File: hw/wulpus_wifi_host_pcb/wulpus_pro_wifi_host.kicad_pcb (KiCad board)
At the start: 2 copper layers, 39 x 20.9 mm, 2 parts, among them J1 DF40C-50DP-0.4V_51_, U1 XIAO-ESP32-C6-SMD

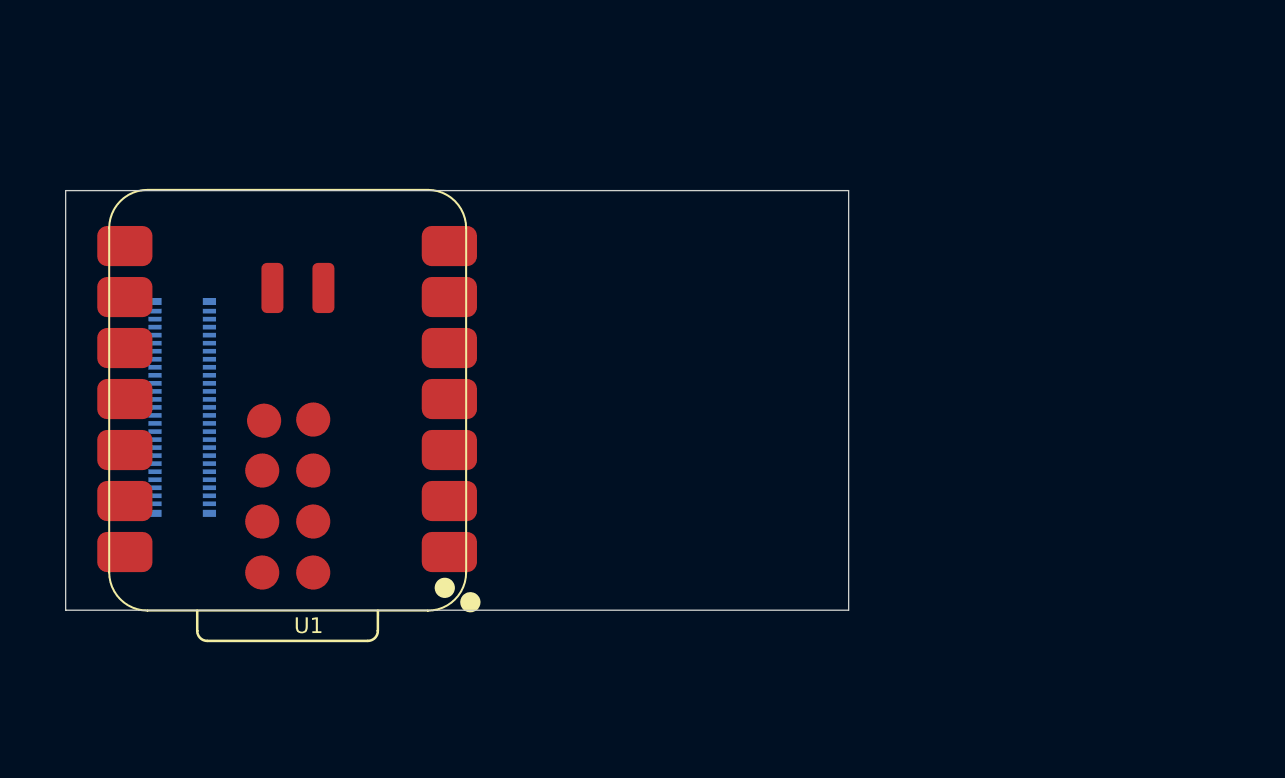
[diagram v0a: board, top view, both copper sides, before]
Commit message: Added main ICs to the schematics and layout template
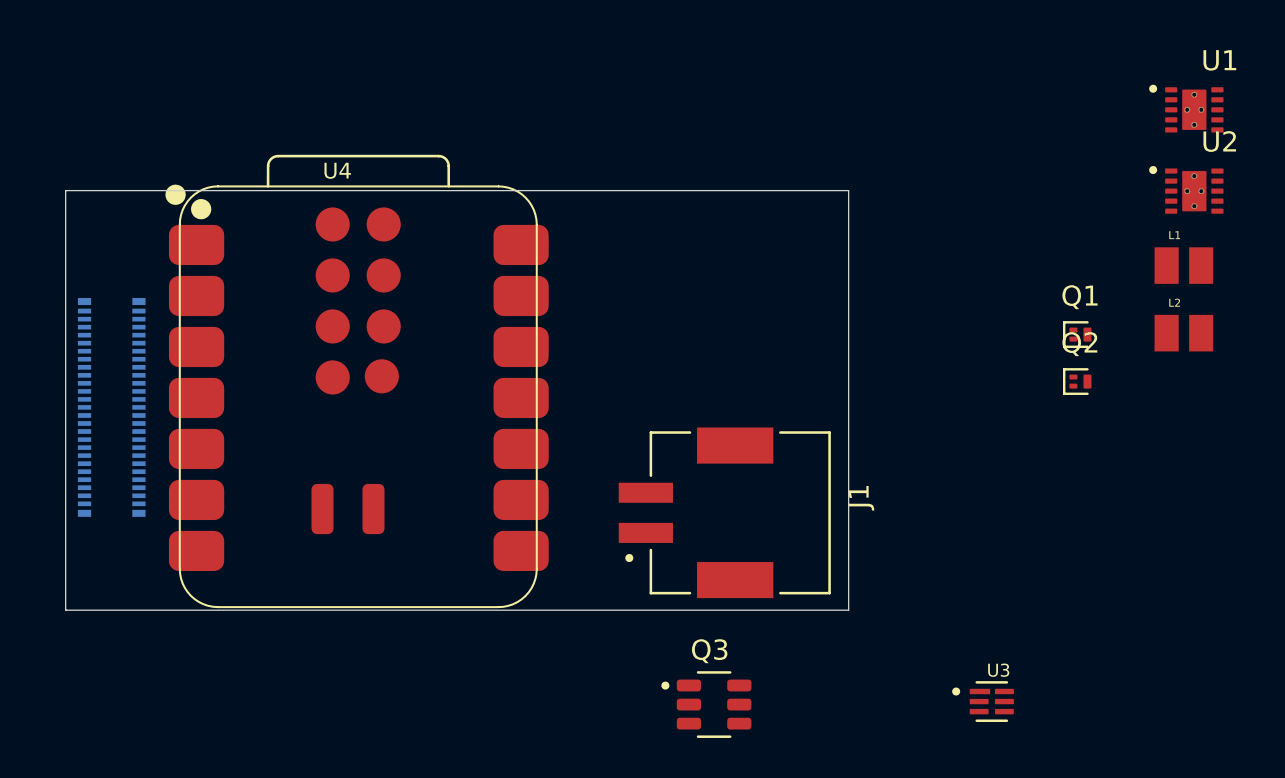
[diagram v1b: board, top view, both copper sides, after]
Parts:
- added J2: DF40C-50DP-0.4V_51_, Ultrasound:HIROSE_DF40C-50DP-0.4V_51_, B.Cu at (67.3, 90.9)
- added L1: DFE201612E-2R2M=P2, Ultrasound:INDC2016X120N, F.Cu at (120.7, 83.8)
- added L2: DFE201612E-2R2M=P2, Ultrasound:INDC2016X120N, F.Cu at (120.7, 87.2)
- added Q1: LP0404N3T5G, Package_TO_SOT_SMD:SOT-883, F.Cu at (115.5, 87.3)
- added Q2: LP0404N3T5G, Package_TO_SOT_SMD:SOT-883, F.Cu at (115.5, 89.6)
- added Q3: FS8205A, Ultrasound:SOT95P280X145-6N, F.Cu at (97.3, 105.7)
- added U2: TPS63900DSKR, Ultrasound:IC_TPS63900DSKR, F.Cu at (121.2, 80.1)
- added U3: BQ29700DSER, Ultrasound:SON50P150X150X80-6N, F.Cu at (111.1, 105.5)
- added U4: XIAO-ESP32-C6-SMD, Ultrasound:XIAO-ESP32-C6-SMD, F.Cu at (70.7, 100.9)
- J1: value DF40C-50DP-0.4V_51_ -> SM02B-PASS-TBT_LF__SN_; footprint Ultrasound:HIROSE_DF40C-50DP-0.4V_51_ -> Ultrasound:JST_SM02B-PASS-TBT_LF__SN_; moved to F.Cu
- U1: value XIAO-ESP32-C6-SMD -> TPS63900DSKR; footprint Ultrasound:XIAO-ESP32-C6-SMD -> Ultrasound:IC_TPS63900DSKR
- moved U1 36.5 mm to (121.2, 76.1), turned to 0 degrees
- moved J1 27.5 mm to (97.8, 96.2)
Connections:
- U1 pad 12: unconnected-(U1-3V3_OUT-Pad12) -> (no net)
- U1 pad 13: unconnected-(U1-GND-Pad13) -> (no net)
- U1 pad 14: unconnected-(U1-VBUS-Pad14) -> (no net)
- U1 pad 15: unconnected-(U1-MTDI-Pad15) -> (no net)

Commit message: Updated footprints, mapped 3D models, added layerstack, partial placement and layout
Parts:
- removed the Q2 at (115.5, 89.6)
- added C1: 22 uF, Capacitor_SMD:C_0402_1005Metric, F.Cu at (99.0, 96.3)
- added C2: 10 uF, Capacitor_SMD:C_0402_1005Metric, F.Cu at (103.0, 95.2)
- added C3: 0.1uF, Capacitor_SMD:C_0402_1005Metric, B.Cu at (94.5, 84.8)
- added C4: 22 uF, Capacitor_SMD:C_0402_1005Metric, F.Cu at (92.8, 96.3)
- added C5: 10 uF, Capacitor_SMD:C_0402_1005Metric, F.Cu at (96.8, 95.2)
- added C6: 100 nF, Capacitor_SMD:C_0402_1005Metric, F.Cu at (90.5, 81.7)
- added C7: 10 uF, Capacitor_SMD:C_0402_1005Metric, B.Cu at (71.5, 94.6)
- added C8: 10 uF, Capacitor_SMD:C_0402_1005Metric, B.Cu at (71.7, 91.5)
- added D1: LMBR4010BST5G, Diode_SMD:D_SOD-882, F.Cu at (90.5, 83.5)
- added R1: 47, Resistor_SMD:R_0402_1005Metric, F.Cu at (68.7, 81.8)
- added R10: 47, Resistor_SMD:R_0402_1005Metric, B.Cu at (72.1, 84.1)
- added R11: 47, Resistor_SMD:R_0402_1005Metric, B.Cu at (72.1, 85.4)
- added R12: 0, Resistor_SMD:R_0402_1005Metric, F.Cu at (101.0, 92.8)
- added R13: o, Resistor_SMD:R_0402_1005Metric, F.Cu at (100.0, 92.8)
- added R14: 2.2k, Resistor_SMD:R_0402_1005Metric, B.Cu at (91.9, 82.1)
- added R15: 16.2k, Resistor_SMD:R_0402_1005Metric, F.Cu at (99.0, 93.8)
- added R16: 5.1M, Resistor_SMD:R_0402_1005Metric, B.Cu at (100.7, 81.5)
- added R17: 5.1M, Resistor_SMD:R_0402_1005Metric, B.Cu at (100.8, 84.1)
- added R18: 0, Resistor_SMD:R_0402_1005Metric, F.Cu at (94.7, 92.8)
- added R19: 330, Resistor_SMD:R_0402_1005Metric, B.Cu at (94.3, 85.8)
- added R2: 47, Resistor_SMD:R_0402_1005Metric, B.Cu at (71.9, 90.0)
- added R20: o, Resistor_SMD:R_0402_1005Metric, F.Cu at (93.8, 92.8)
- added R21: 36.5k, Resistor_SMD:R_0402_1005Metric, F.Cu at (92.8, 93.8)
- added R22: 100k, Resistor_SMD:R_0402_1005Metric, F.Cu at (91.8, 82.5)
- added R23: 100, Resistor_SMD:R_0402_1005Metric, F.Cu at (92.8, 83.3)
- added R3: 47, Resistor_SMD:R_0402_1005Metric, F.Cu at (69.2, 87.5)
- added R4: 47, Resistor_SMD:R_0402_1005Metric, F.Cu at (69.2, 90.0)
- added R5: 47, Resistor_SMD:R_0402_1005Metric, F.Cu at (69.1, 92.6)
- added R6: 47, Resistor_SMD:R_0402_1005Metric, F.Cu at (69.1, 95.1)
- added R7: 47, Resistor_SMD:R_0402_1005Metric, F.Cu at (68.6, 98.2)
- added R8: 47, Resistor_SMD:R_0402_1005Metric, B.Cu at (72.1, 82.8)
- added R9: 47, Resistor_SMD:R_0402_1005Metric, B.Cu at (72.1, 81.4)
- added TP1: TestPoint, TestPoint:TestPoint_Pad_1.0x1.0mm, F.Cu at (98.4, 98.9)
- added TP2: TestPoint, TestPoint:TestPoint_Pad_1.0x1.0mm, F.Cu at (92.2, 98.8)
- added TP3: TestPoint, TestPoint:TestPoint_Pad_1.0x1.0mm, F.Cu at (110.7, 89.0)
- added TP4: TestPoint, TestPoint:TestPoint_Pad_1.0x1.0mm, F.Cu at (67.8, 84.7)
- added TP5: TestPoint, TestPoint:TestPoint_Pad_1.0x1.0mm, F.Cu at (107.0, 89.3)
- J1: value SM02B-PASS-TBT_LF__SN_ -> S2B-PH-SM4-TB_LF__SN_; footprint Ultrasound:JST_SM02B-PASS-TBT_LF__SN_ -> Ultrasound:JST_S2B-PH-SM4-TB_LF__SN_
- Q1: renamed from Q3; moved to B.Cu
- U3: moved to B.Cu
- moved U4 32.8 mm to (94.8, 95.5), turned to -90 degrees
- moved U3 29.3 mm to (93.9, 81.8), turned to -90 degrees
- moved L2 28.2 mm to (95.0, 98.8)
- moved U2 25.4 mm to (101.0, 95.5), turned to -90 degrees
- moved L1 24.7 mm to (101.1, 98.8)
- moved Q2 24.0 mm to (91.8, 84.3), turned to -90 degrees
- moved Q1 23.7 mm to (97.3, 82.0)
- moved J1 8.38 mm to (98.5, 87.8), turned to 180 degrees
- moved J2 0.97 mm to (67.7, 90.0)
- moved U1 0.32 mm to (71.0, 101.1)
- renumbered Q1 to Q2, U4 to U1, U1 to U4
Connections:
- J1 pad 1: unconnected-(J1-Pad1) -> /Power/VBAT
- J1 pad 2: unconnected-(J1-Pad2) -> Net-(U3-VSS)
- J1 pad S1: Net-(J1-SHIELD-PadS1) -> GND
- J1 pad S2: Net-(J1-SHIELD-PadS1) -> GND
- J2 pad 1: unconnected-(J2-Pad1) -> /b2b_connector Sheet/SPI.MOSI
- J2 pad 15: unconnected-(J2-Pad15) -> GND
- J2 pad 16: unconnected-(J2-Pad16) -> GND
- J2 pad 2: unconnected-(J2-Pad2) -> /b2b_connector Sheet/SPI.MISO
- J2 pad 22: unconnected-(J2-Pad22) -> /b2b_connector Sheet/MSP_JTAG.TEST
- J2 pad 24: unconnected-(J2-Pad24) -> Net-(J2-Pad24)
- J2 pad 25: unconnected-(J2-Pad25) -> /b2b_connector Sheet/data_rdy
- J2 pad 26: unconnected-(J2-Pad26) -> /b2b_connector Sheet/MSP_JTAG.TDO
- J2 pad 28: unconnected-(J2-Pad28) -> /b2b_connector Sheet/MSP_JTAG.TDI
- J2 pad 29: unconnected-(J2-Pad29) -> +3V3
- J2 pad 3: unconnected-(J2-Pad3) -> /b2b_connector Sheet/SPI.SS
- J2 pad 30: unconnected-(J2-Pad30) -> /b2b_connector Sheet/MSP_JTAG.TMS
- J2 pad 31: unconnected-(J2-Pad31) -> +3V3
- J2 pad 33: unconnected-(J2-Pad33) -> +5V
- J2 pad 36: unconnected-(J2-Pad36) -> GND
- J2 pad 37: unconnected-(J2-Pad37) -> +3V3 ESP
- J2 pad 39: unconnected-(J2-Pad39) -> +3V3 ESP
- J2 pad 4: unconnected-(J2-Pad4) -> /b2b_connector Sheet/SPI.CLK
- J2 pad 47: unconnected-(J2-Pad47) -> +V_board
- J2 pad 48: unconnected-(J2-Pad48) -> /b2b_connector Sheet/MSP_JTAG.TCK
- J2 pad 49: unconnected-(J2-Pad49) -> +V_board
- J2 pad 50: unconnected-(J2-Pad50) -> /b2b_connector Sheet/MSP_JTAG.RST_n
- L1 pad 1: unconnected-(L1-Pad1) -> Net-(U2-LX2)
- L1 pad 2: unconnected-(L1-Pad2) -> Net-(U2-LX1)
- L2 pad 1: unconnected-(L2-Pad1) -> Net-(U4-LX2)
- L2 pad 2: unconnected-(L2-Pad2) -> Net-(U4-LX1)
- Q1 pad 1: unconnected-(Q3-Pad1) -> Net-(U3-VSS)
- Q1 pad 3: unconnected-(Q3-Pad3) -> GND
- Q1 pad 4: unconnected-(Q3-Pad4) -> Net-(U3-COUT)
- Q1 pad 6: unconnected-(Q3-Pad6) -> Net-(U3-DOUT)
- Q2 pad 1: unconnected-(Q1-G-Pad1) -> Net-(Q2-G)
- Q2 pad 2: unconnected-(Q1-S-Pad2) -> +V_board
- Q2 pad 3: unconnected-(Q1-D-Pad3) -> /Power/VBAT
- U1 pad 1: unconnected-(U4-D0-Pad1) -> Net-(U1-D0)
- U1 pad 10: unconnected-(U4-D9-Pad10) -> Net-(U1-D9)
- U1 pad 11: unconnected-(U4-D10-Pad11) -> Net-(U1-D10)
- U1 pad 12: unconnected-(U4-3V3_OUT-Pad12) -> +3V3 ESP
- U1 pad 13: unconnected-(U4-GND-Pad13) -> GND
- U1 pad 14: unconnected-(U4-VBUS-Pad14) -> /Power/VBUS
- U1 pad 2: unconnected-(U4-D1-Pad2) -> Net-(U1-D1)
- U1 pad 23: unconnected-(U4-VBAT-Pad23) -> /Power/VBAT
- U1 pad 24: unconnected-(U4-GND-Pad24) -> GND
- U1 pad 3: unconnected-(U4-D2-Pad3) -> Net-(U1-D2)
- U1 pad 4: unconnected-(U4-D3-Pad4) -> Net-(U1-D3)
- U1 pad 5: unconnected-(U4-D4-Pad5) -> Net-(U1-D4)
- U1 pad 6: unconnected-(U4-D5-Pad6) -> Net-(U1-D5)
- U1 pad 7: unconnected-(U4-D6-Pad7) -> Net-(U1-D6)
- U1 pad 8: unconnected-(U4-D7-Pad8) -> Net-(U1-D7)
- U1 pad 9: unconnected-(U4-D8-Pad9) -> Net-(U1-D8)
- U2 pad 1: unconnected-(U2-EN-Pad1) -> +V_board
- U2 pad 10: unconnected-(U2-VIN-Pad10) -> +V_board
- U2 pad 11: unconnected-(U2-EXP-Pad11) -> GND
- U2 pad 2: unconnected-(U2-SEL-Pad2) -> GND
- U2 pad 3: unconnected-(U2-CFG1-Pad3) -> Net-(U2-CFG1)
- U2 pad 4: unconnected-(U2-CFG2-Pad4) -> Net-(U2-CFG2)
- U2 pad 5: unconnected-(U2-CFG3-Pad5) -> Net-(U2-CFG3)
- U2 pad 6: unconnected-(U2-VOUT-Pad6) -> +3V3
- U2 pad 7: unconnected-(U2-LX2-Pad7) -> Net-(U2-LX2)
- U2 pad 8: unconnected-(U2-GND-Pad8) -> GND
- U2 pad 9: unconnected-(U2-LX1-Pad9) -> Net-(U2-LX1)
- U3 pad 2: unconnected-(U3-COUT-Pad2) -> Net-(U3-COUT)
- U3 pad 3: unconnected-(U3-DOUT-Pad3) -> Net-(U3-DOUT)
- U3 pad 4: unconnected-(U3-VSS-Pad4) -> Net-(U3-VSS)
- U3 pad 5: unconnected-(U3-BAT-Pad5) -> Net-(U3-BAT)
- U3 pad 6: unconnected-(U3-V--Pad6) -> Net-(U3-V-)
- U4 pad 1: unconnected-(U1-EN-Pad1) -> +V_board
- U4 pad 10: unconnected-(U1-VIN-Pad10) -> +V_board
- U4 pad 11: unconnected-(U1-EXP-Pad11) -> GND
- U4 pad 2: unconnected-(U1-SEL-Pad2) -> GND
- U4 pad 3: unconnected-(U1-CFG1-Pad3) -> Net-(U4-CFG1)
- U4 pad 4: unconnected-(U1-CFG2-Pad4) -> Net-(U4-CFG2)
- U4 pad 5: unconnected-(U1-CFG3-Pad5) -> Net-(U4-CFG3)
- U4 pad 6: unconnected-(U1-VOUT-Pad6) -> +5V
- U4 pad 7: unconnected-(U1-LX2-Pad7) -> Net-(U4-LX2)
- U4 pad 8: unconnected-(U1-GND-Pad8) -> GND
- U4 pad 9: unconnected-(U1-LX1-Pad9) -> Net-(U4-LX1)
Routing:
- net /Power/VBAT: track 0.00 -> 39.5 mm
- net Net-(U1-D9): track 0.00 -> 25.1 mm, vias 0 -> 1
- net Net-(U1-D7): track 0.00 -> 24.0 mm, vias 0 -> 1
- net Net-(U1-D8): track 0.00 -> 23.6 mm, vias 0 -> 1
- net Net-(U1-D10): track 0.00 -> 23.4 mm, vias 0 -> 1
- net /b2b_connector Sheet/MSP_JTAG.RST_n: track 0.00 -> 16.5 mm, vias 0 -> 1
- net /b2b_connector Sheet/SPI.MISO: track 0.00 -> 7.65 mm
- net /b2b_connector Sheet/SPI.CLK: track 0.00 -> 6.92 mm
- net Net-(J2-Pad24): track 0.00 -> 6.87 mm, vias 0 -> 1
- net Net-(U1-D1): track 0.00 -> 5.99 mm, vias 0 -> 1
- net /b2b_connector Sheet/MSP_JTAG.TMS: track 0.00 -> 5.22 mm, vias 0 -> 1
- net /b2b_connector Sheet/MSP_JTAG.TCK: track 0.00 -> 5.04 mm, vias 0 -> 1
- net /b2b_connector Sheet/MSP_JTAG.TEST: track 0.00 -> 3.85 mm, vias 0 -> 1
- net /b2b_connector Sheet/MSP_JTAG.TDI: track 0.00 -> 3.45 mm, vias 0 -> 1
- net Net-(U1-D0): track 0.00 -> 3.15 mm
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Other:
- board size 39 x 20.9 mm -> 39 x 21 mm
- copper layers 2 -> 4

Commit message: Added preliminary layout
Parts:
- moved TP3 14.0 mm to (97.0, 92.2)
- moved TP5 4.89 mm to (102.2, 90.0)
- moved R14 3.22 mm to (93.7, 84.8)
- moved U3 3.21 mm to (95.5, 84.7)
- moved Q1 3.18 mm to (99.3, 84.5)
- moved R17 3.06 mm to (99.3, 86.8)
- moved C3 3.01 mm to (95.3, 87.7)
- moved R16 1.52 mm to (99.4, 82.3), turned to 180 degrees
- moved C6 1.45 mm to (90.5, 83.2)
- moved D1 1.45 mm to (90.5, 84.9)
- moved Q2 1.45 mm to (91.8, 85.8)
- moved R23 1.45 mm to (92.8, 84.8)
- moved R22 1.45 mm to (91.8, 84.0)
- moved R15 1.00 mm to (99.0, 92.8)
- moved C1 0.82 mm to (98.9, 95.5)
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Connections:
- U2 pad 12: (no net) -> GND
- U2 pad 13: (no net) -> GND
- U4 pad 12: (no net) -> GND
- U4 pad 13: (no net) -> GND
- U4 pad 14: (no net) -> GND
- U4 pad 15: (no net) -> GND
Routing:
- net Net-(U3-DOUT): track 0.00 -> 11.5 mm, vias 0 -> 2
- net Net-(Q1-Pad2): track 0.00 -> 10.3 mm, vias 0 -> 1
- net Net-(U3-COUT): track 0.00 -> 9.61 mm
- net GND: track 0.00 -> 6.19 mm, vias 0 -> 43
- net +5V: track 0.00 -> 6.02 mm, vias 0 -> 2
- net +V_board: track 0.00 -> 5.28 mm, vias 0 -> 12
- net +3V3 ESP: track 0.00 -> 5.26 mm, vias 0 -> 4
- net Net-(U3-VSS): track 0.00 -> 3.71 mm, vias 0 -> 7
- net +3V3: track 0.00 -> 3.22 mm, vias 0 -> 4
- net Net-(U3-BAT): track 0.00 -> 2.64 mm
- net Net-(U2-CFG3): track 0.00 -> 1.44 mm
- net Net-(U4-CFG2): track 0.00 -> 1.32 mm
- net Net-(U3-V-): track 0.00 -> 1.26 mm
- net Net-(U2-CFG2): track 0.00 -> 1.22 mm
- net Net-(U4-CFG1): track 0.00 -> 1.13 mm
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- added copper zone on B.Cu, net +3V3
- added copper zone on F.Cu, net +3V3
- added copper zone on In2.Cu, net +3V3
- added copper zone on B.Cu, net +3V3 ESP
- added copper zone on In2.Cu, net +3V3 ESP
- added copper zone on In2.Cu, net +5V
- added copper zone on B.Cu, net +V_board
- added copper zone on F.Cu, net +V_board
- added copper zone on In2.Cu, net +V_board
- added copper zone on F.Cu, net /Power/VBUS
- added copper zone on B.Cu, net GND
- added copper zone on F.Cu, net GND
- added copper zone on In1.Cu, net GND
- added copper zone on In2.Cu, net GND
- added copper zone on F.Cu, net Net-(U2-LX1)
- added copper zone on F.Cu, net Net-(U2-LX2)
- added copper zone on B.Cu, net Net-(U3-VSS)
- added copper zone on F.Cu, net Net-(U3-VSS)
- added copper zone on F.Cu, net Net-(U4-LX1)
- added copper zone on F.Cu, net Net-(U4-LX2)
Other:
- rule pad_to_mask_clearance: 0 -> 0.1

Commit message: Finished layout, fixed DRCs
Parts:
- added QR*****: https://github.com/Sergio5714/wulpus-pro, Ultrasound:wulpus_pro_qr, B.Cu at (83.0, 86.9)
- added TP6: TestPoint, TestPoint:TestPoint_Pad_1.0x1.0mm, F.Cu at (91.5, 90.7)
- added TP7: TestPoint, TestPoint:TestPoint_Pad_1.0x1.0mm, F.Cu at (66.6, 97.1)
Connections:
- U2 pad 14: (no net) -> GND
- U2 pad 15: (no net) -> GND
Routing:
- net GND: track 6.19 -> 4.77 mm
- net +3V3 ESP: track 5.26 -> 4.21 mm
- net /Power/VBAT: track 40.3 -> 39.3 mm
- net Net-(U1-D3): track 3.14 -> 2.28 mm
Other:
- board text added: "WiFi Host Board v1.0 Sergei Vostrikov 29.07.26"

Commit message: Changed cap footprints to 0603
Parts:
- C1, C2, C4, C5, C7, C8: footprint Capacitor_SMD:C_0402_1005Metric -> Capacitor_SMD:C_0603_1608Metric
- R13, R20: value o -> 0
- moved C4 1.32 mm to (91.8, 95.4)
- moved R21 1.17 mm to (92.1, 92.8)
- moved TP2 0.78 mm to (91.4, 98.9)
- moved L2 0.72 mm to (94.2, 98.9)
- moved R18 0.72 mm to (94.0, 92.8)
- moved R20 0.72 mm to (93.0, 92.8)
- moved U4 0.72 mm to (94.1, 95.6)
- moved C1 0.62 mm to (98.4, 95.3)
- moved TP3 0.59 mm to (96.5, 92.2)
- moved C5 0.51 mm to (96.3, 95.3)
- moved TP1 0.44 mm to (98.0, 98.9)
- moved L1 0.44 mm to (100.7, 98.9)
- moved R12 0.44 mm to (100.6, 92.9)
- moved R13 0.44 mm to (99.6, 92.9)
- moved R15 0.44 mm to (98.6, 92.9)
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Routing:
- net +V_board: track 5.22 -> 7.71 mm, vias 12 -> 11
- net +5V: track 6.02 -> 4.70 mm
- net Net-(U4-CFG3): track 0.96 -> 1.52 mm
- net GND: vias 43 -> 47
- added copper zone on F.Cu, net +5V
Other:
- board text added: "WiFi Host Board v1.0 Sergei Vostrikov 30.07.26"
- board text removed: "WiFi Host Board v1.0 Sergei Vostrikov 29.07.26"

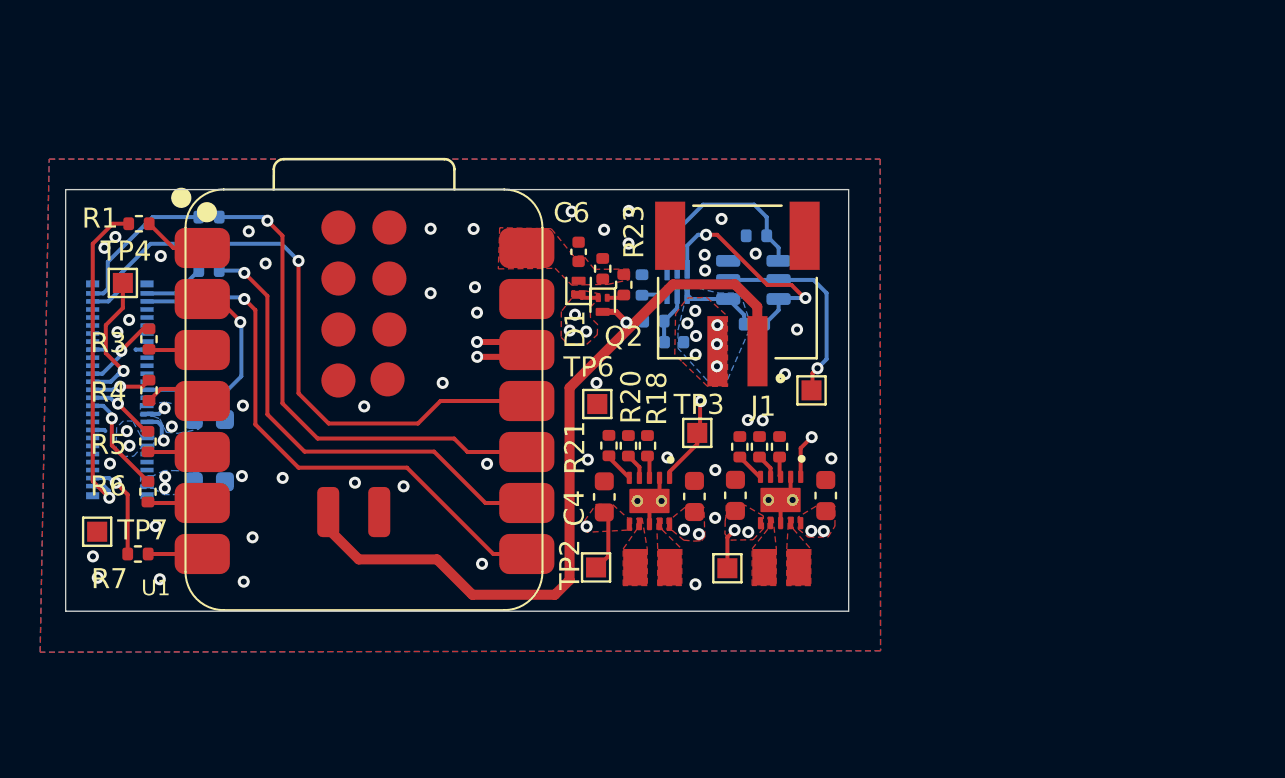
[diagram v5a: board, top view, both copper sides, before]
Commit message: Added out capacitors for DC-DCs, regenerated fabrication files
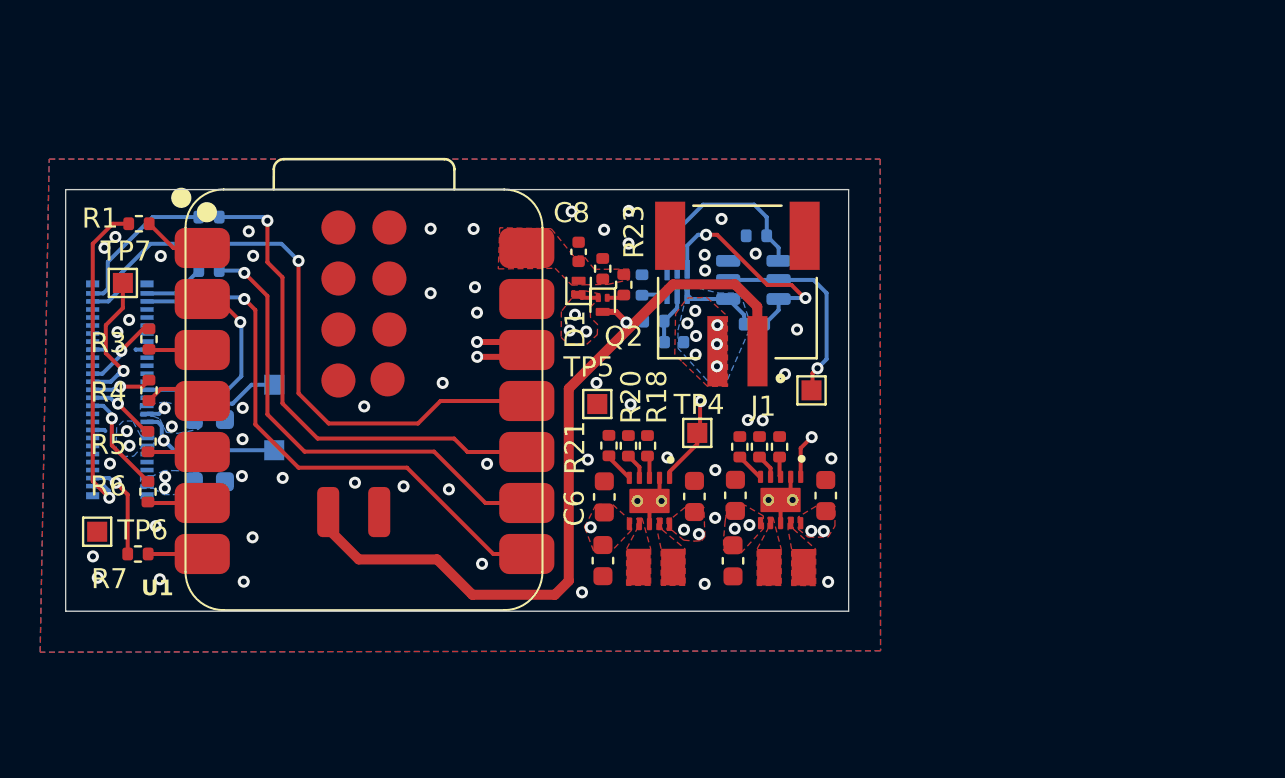
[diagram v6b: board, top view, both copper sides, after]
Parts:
- removed the TP1 at (98.0, 98.9)
- added C1: 22 uF, Capacitor_SMD:C_0603_1608Metric, F.Cu at (98.2, 98.5)
- added C5: 22 uF, Capacitor_SMD:C_0603_1608Metric, F.Cu at (91.8, 98.5)
- added TP2: TestPoint, TestPoint:TestPoint_Pad_1.0x1.0mm, B.Cu at (75.4, 89.8)
- C4: renamed from C3; value 0.1uF -> 100 nF
- TP3: renamed from TP2; moved to B.Cu
- moved TP3 17.1 mm to (75.4, 93.0), turned to 180 degrees
- moved L1 0.24 mm to (100.9, 98.9)
- moved L2 0.17 mm to (94.4, 98.8)
- renumbered C8 to C10, C1 to C2, C2 to C3, C4 to C6, C5 to C7, C6 to C8, C7 to C9, TP5 to TP1, TP3 to TP4, TP6 to TP5, TP7 to TP6, TP4 to TP7
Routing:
- net +5V: track 4.70 -> 7.77 mm
- net +3V3: track 3.04 -> 5.71 mm
- net GND: vias 47 -> 52
